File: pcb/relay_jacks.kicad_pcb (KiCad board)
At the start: 2 copper layers, 30.5 x 35.8 mm, 26 parts, among them J1 AudioJack3_Ground, J2 Conn_01x03, J3 Conn_01x02, J4 Conn_01x02, J5 AudioJack3_Ground, J6 AudioJack3_Ground, K1 Y14x-1C-xxDS, K2 Y14x-1C-xxDS, K3 Y14x-1C-xxDS, Q1 Q_NMOS_GSD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

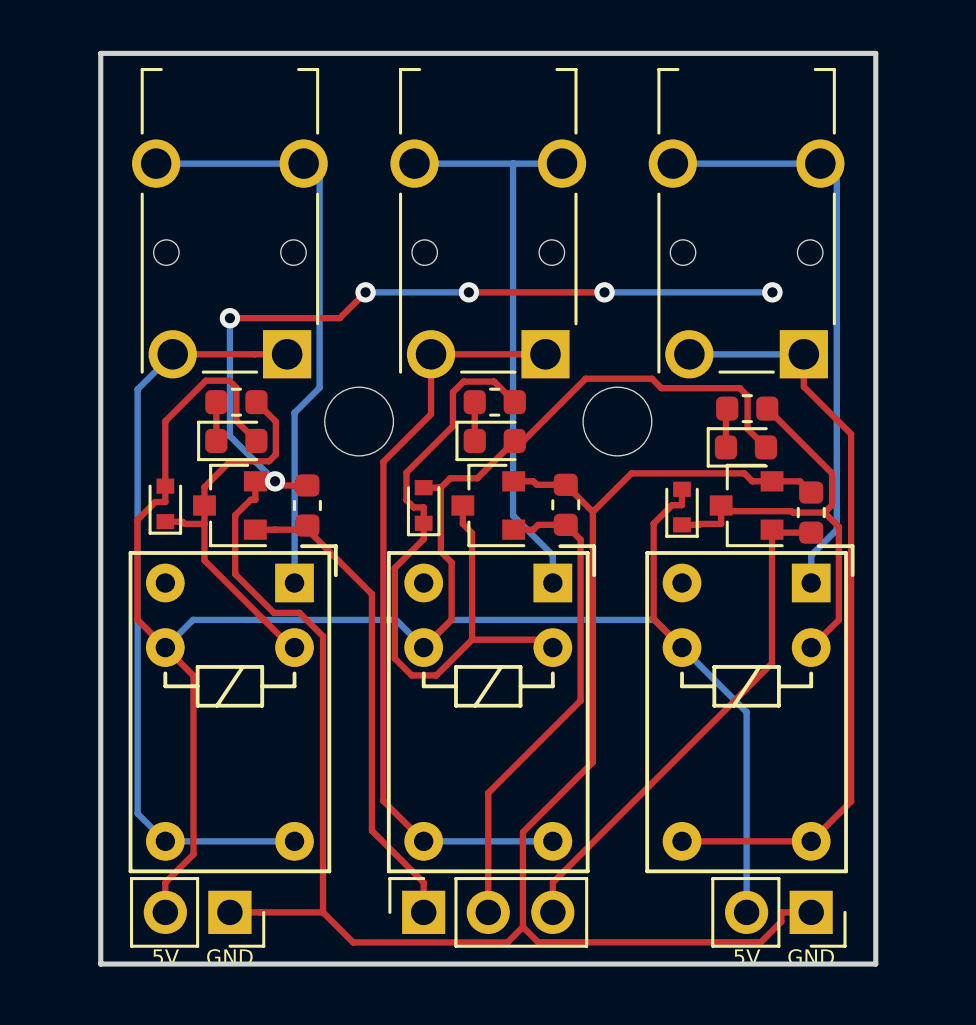
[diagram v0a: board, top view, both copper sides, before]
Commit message: Update pcb design as rev 2018.11
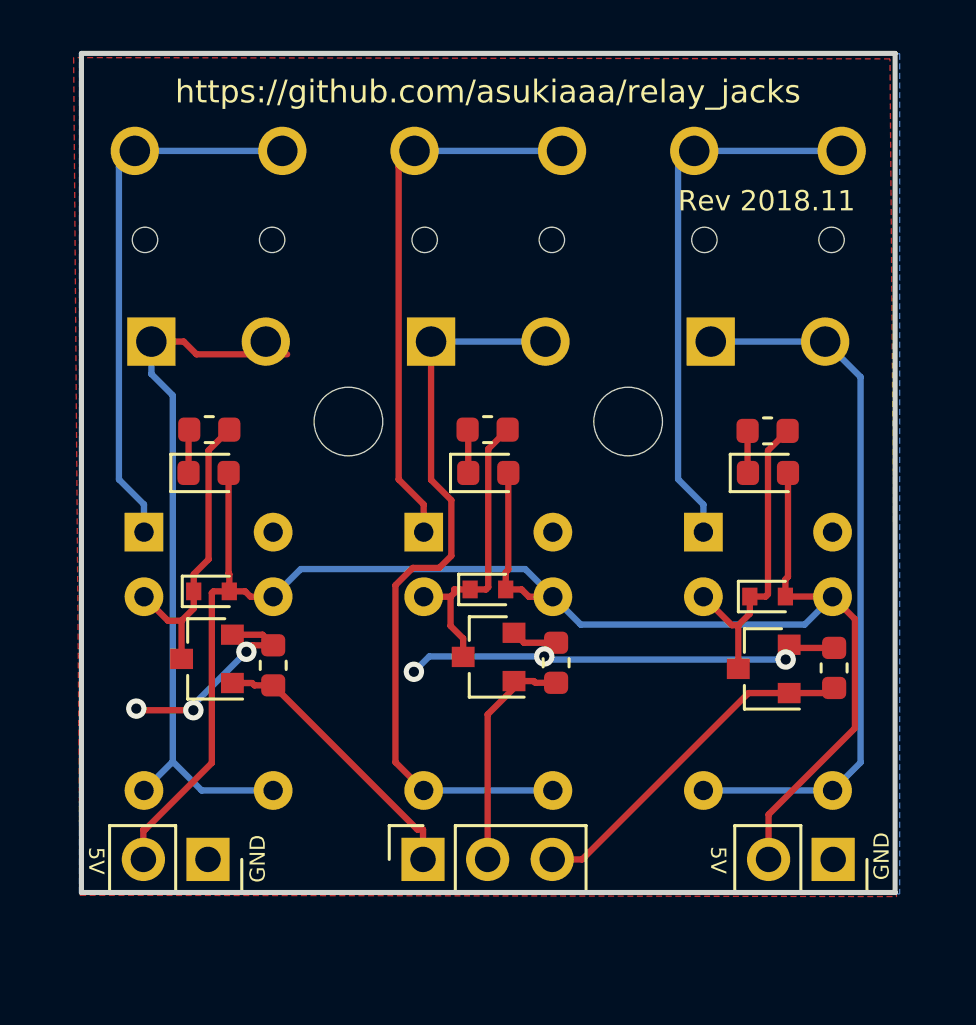
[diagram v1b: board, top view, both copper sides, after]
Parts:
- J1, J5, J6, K1, K2, K3: moved to B.Cu
- moved Q3 6.46 mm to (99.2, 111.1)
- moved R2 6.43 mm to (79.9, 110.9)
- moved K1 6.25 mm to (74.9, 105.7)
- moved R3 6.22 mm to (91.1, 110.8)
- moved R5 6.17 mm to (102.0, 111.0)
- moved Q1 6.10 mm to (77.3, 110.7)
- moved Q2 5.96 mm to (88.4, 110.6)
- moved K2 5.46 mm to (85.9, 105.7)
- moved D6 4.87 mm to (99.4, 108.2), turned to 0 degrees
- moved K3 4.69 mm to (96.9, 105.7)
- moved D4 4.16 mm to (88.4, 108.0), turned to 0 degrees
- moved D2 3.89 mm to (77.5, 108.0), turned to 0 degrees
- moved J4 2.26 mm to (102.0, 118.6)
- moved J3 2.25 mm to (77.4, 118.6)
- moved J2 2.08 mm to (85.8, 118.6)
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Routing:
- net GND: track 105.6 -> 27.9 mm
- net +5V: track 92.4 -> 68.1 mm
- net Net-(D4-Pad1): track 27.8 -> 11.9 mm
- net SIG1: track 19.1 -> 9.24 mm
- net SIG0: track 19.2 -> 11.1 mm
- net SIG2: track 20.2 -> 13.9 mm
- net Net-(D6-Pad1): track 17.6 -> 12.4 mm
- net Net-(D2-Pad1): track 15.1 -> 11.7 mm
- net Net-(J6-Pad2): track 30.2 -> 28.3 mm
- net Net-(J6-Pad4): track 23.0 -> 21.5 mm
- net Net-(J1-Pad4): track 23.0 -> 21.5 mm
- net Net-(J5-Pad4): track 22.9 -> 21.5 mm
- net Net-(J1-Pad2): track 29.8 -> 29.0 mm
- net Net-(J5-Pad2): track 30.2 -> 29.5 mm
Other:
- board size 30.5 x 35.8 mm -> 32 x 33 mm
- board text added: "Rev 2018.11"
- board text removed: "Rev 2018.10"
